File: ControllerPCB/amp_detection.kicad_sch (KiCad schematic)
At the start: 20 parts

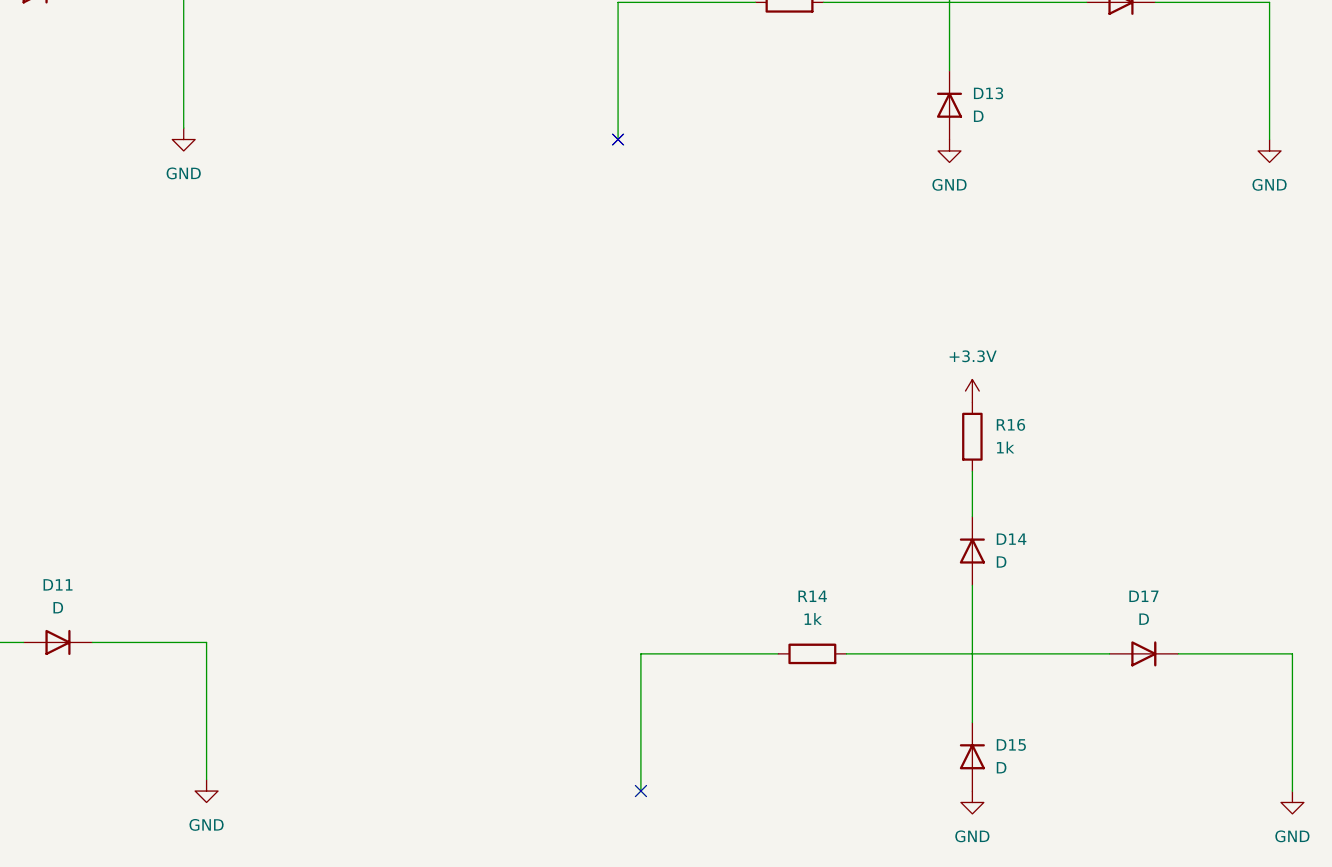
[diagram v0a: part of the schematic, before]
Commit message: Organized the schematic a bit
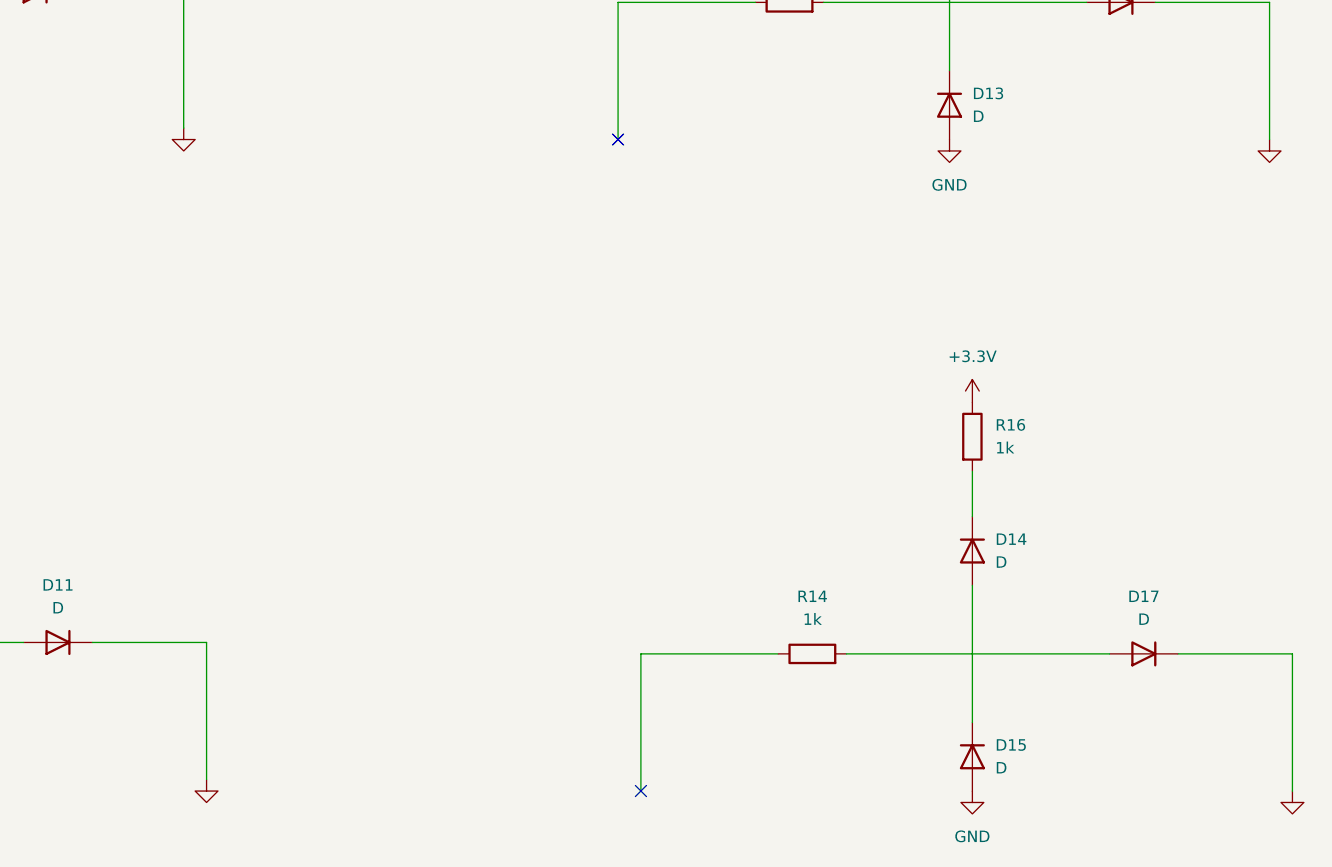
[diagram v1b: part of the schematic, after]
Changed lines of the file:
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@@
 					(size 1.27 1.27)
 				)
+				(hide yes)
 			)
 		)
@@
 					(size 1.27 1.27)
 				)
+				(hide yes)
 			)
 		)
@@
 					(size 1.27 1.27)
 				)
+				(hide yes)
 			)
 		)
@@
 					(size 1.27 1.27)
 				)
-			)
-		)
+				(hide yes)
+			)
+		)

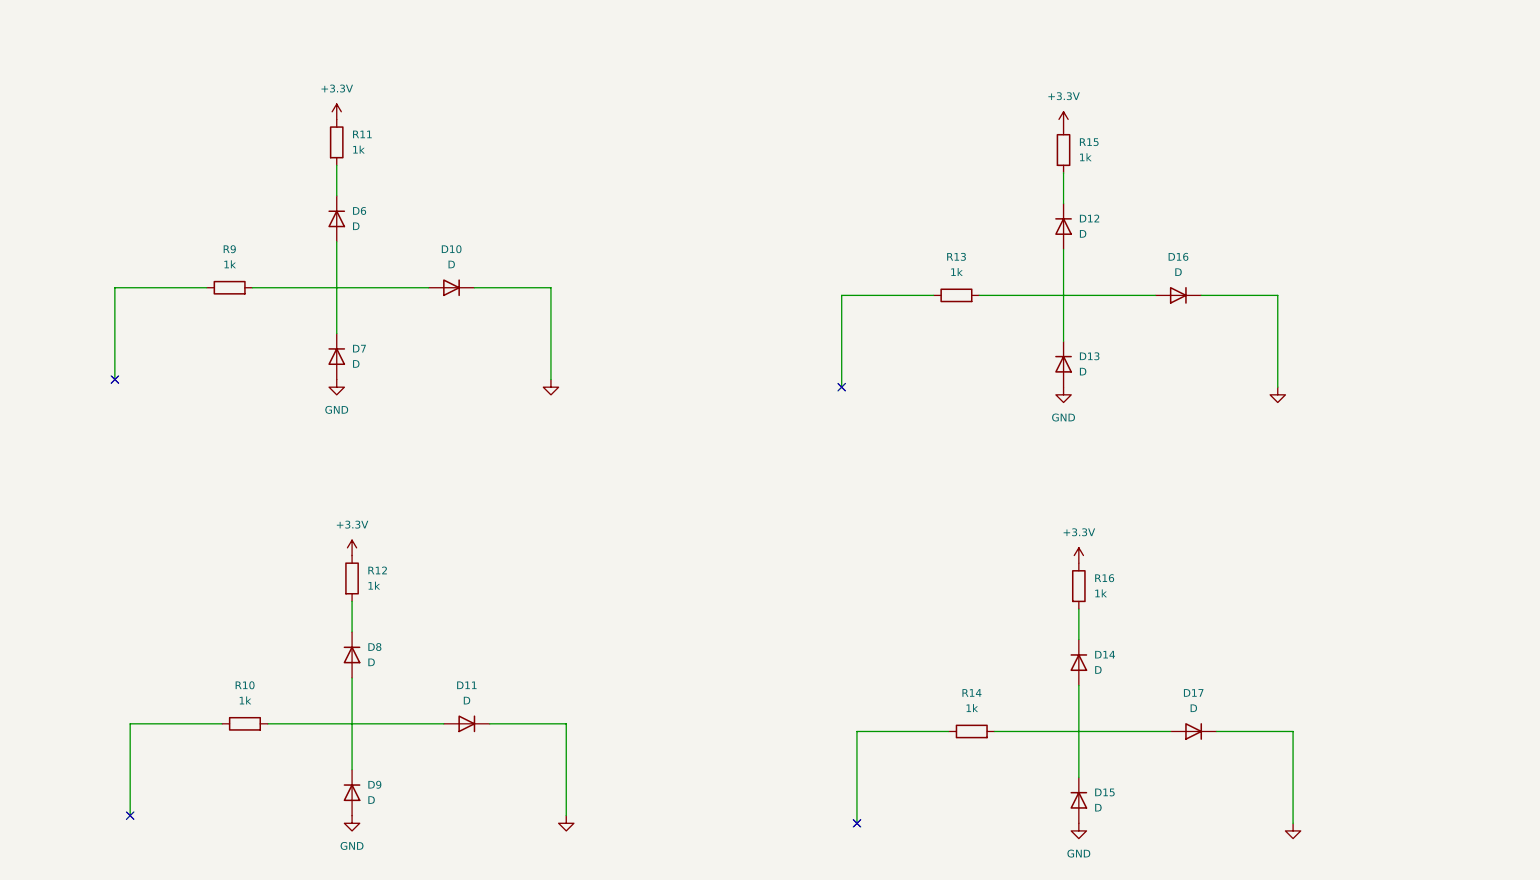
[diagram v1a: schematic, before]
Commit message: Began the PCB. Placed the decoupling caps, usb micro b conn and others. Adding footprints for components as well.
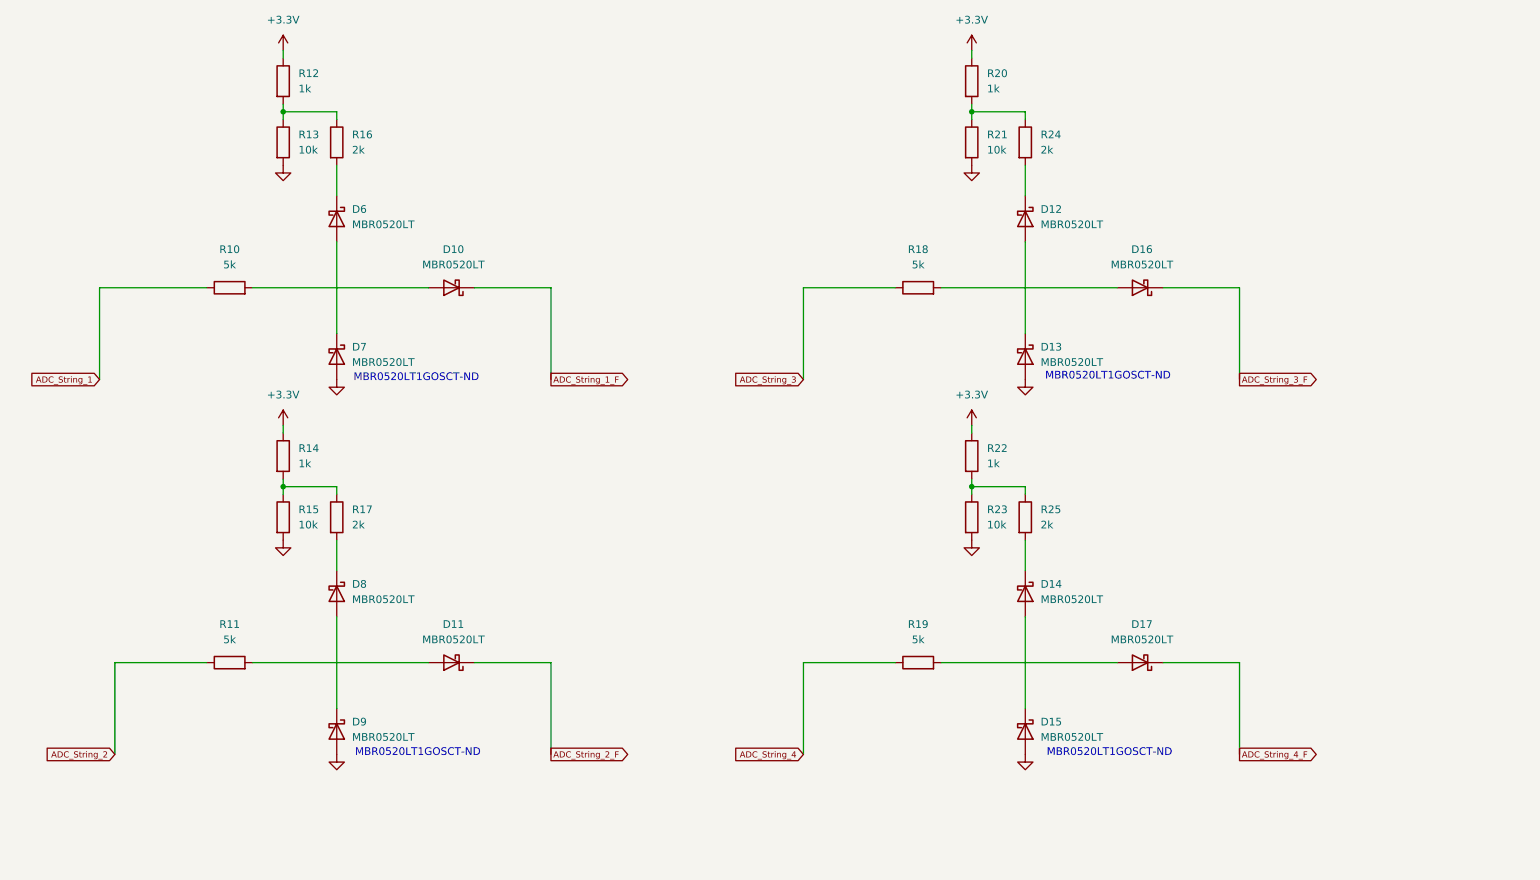
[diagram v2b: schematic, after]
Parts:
- removed D10, D11, D12, D13, D14, D15, D16, D17, D6, D7, D8, D9: D, symbol Device:D
- removed R10, R16: 1k, symbol Device:R
- added D10, D11, D12, D13, D14, D15, D16, D17, D6, D7, D8, D9: MBR0520LT, Diode_SMD:D_SOD-123, symbol Diode:MBR0520LT
- added R11, R18, R19: 5k, Resistor_SMD:R_0402_1005Metric, symbol Device:R
- added R17, R24, R25: 2k, Resistor_SMD:R_0402_1005Metric, symbol Device:R
- added R20, R22: 1k, Resistor_SMD:R_0402_1005Metric, symbol Device:R
- added R21, R23: 10k, Resistor_SMD:R_0402_1005Metric, symbol Device:R
- R10: renamed from R9; value 1k -> 5k; footprint (none) -> Resistor_SMD:R_0402_1005Metric
- R12, R14: footprint (none) -> Resistor_SMD:R_0402_1005Metric
- R13, R15: value 1k -> 10k; footprint (none) -> Resistor_SMD:R_0402_1005Metric
- R16: renamed from R11; value 1k -> 2k; footprint (none) -> Resistor_SMD:R_0402_1005Metric
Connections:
- net +3.3V: now also R14.1, R20.1, R22.1; no longer R15.1, R16.1
- net GND: now also R13.2, R15.2, D13.2 (A), D15.2 (A), D7.2 (A), D9.2 (A), R21.2, R23.2
- net at R16.2: now also D6.1 (K)
- net at R13.1: now also R12.2, R16.1
- net ADC_String_1: now reaches R10.1
- net at R10.2: now also D10.2 (A)
- net at R14.2: now also R15.1, R17.1
- new net: R22.2, R23.1, R25.1
- new net: D8.2 (A), D9.1 (K)
- new net: D17.2 (A), R19.2
- new net: D11.2 (A), R11.2
- new net: D14.2 (A), D15.1 (K)
- new net: D12.1 (K), R24.2
- new net: D12.2 (A), D13.1 (K)
- new net: D8.1 (K), R17.2
- new net: D14.1 (K), R25.2
- new net: D6.2 (A), D7.1 (K)
- new net: R20.2, R21.1, R24.1
- new net: D16.2 (A), R18.2
- new net ADC_String_1_F: D10.1 (K)
- new net ADC_String_2: R11.1
- new net ADC_String_2_F: D11.1 (K)
- new net ADC_String_3: R18.1
- new net ADC_String_3_F: D16.1 (K)
- new net ADC_String_4: R19.1
- new net ADC_String_4_F: D17.1 (K)
- no-connect marks 4 -> 0
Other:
- note added: "MBR0520LT1GOSCT-ND"

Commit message: Added separate sheet for IO. Added TVS diodes for every external input to the controller except for the ADC and MIDI control inputs. Still need to add decoupling caps for the 9V humbucker source. Parts were chosen with JLPCB library stock in mind. Replaced the 8MHz crystal with a 16MHz crystal.
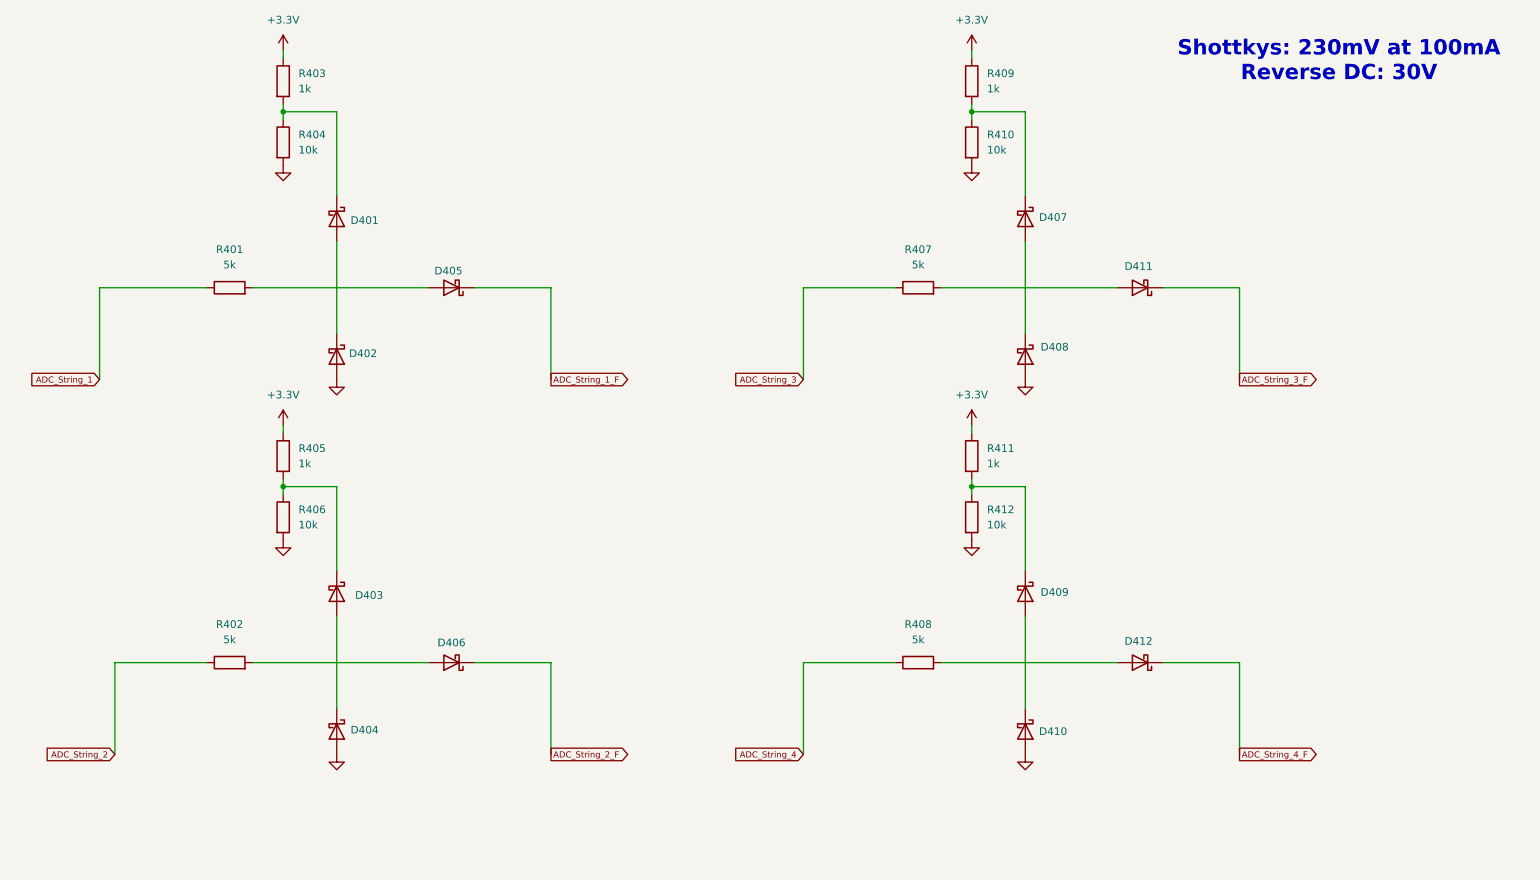
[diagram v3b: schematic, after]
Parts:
- removed R16, R17, R24, R25: 2k, Resistor_SMD:R_0402_1005Metric, symbol Device:R
- renumbered D6 to D401, D7 to D402, D8 to D403, D9 to D404, D10 to D405, D11 to D406, D12 to D407, D13 to D408, D14 to D409, D15 to D410, D16 to D411, D17 to D412, R10 to R401, R11 to R402, R12 to R403, R13 to R404, R14 to R405, R15 to R406, R18 to R407, R19 to R408, R20 to R409, R21 to R410, R22 to R411, R23 to R412
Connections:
- net at R411.2, R412.1: now also D409.1 (K)
- net at R403.2, R404.1: now also D401.1 (K)
- net at D407.1 (K): now also R409.2, R410.1
- net at R405.2, R406.1: now also D403.1 (K)
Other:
- note added: "Shottkys: 230mV at 100mA Reverse DC: 30V"
- note removed: "MBR0520LT1GOSCT-ND"

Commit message: rev 0.3
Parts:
- removed D401, D402, D403, D404, D405, D406, D407, D408, D409, D410, D411, D412: MBR0520LT, Diode_SMD:D_SOD-123, symbol Diode:MBR0520LT
- removed R402: 5k, Resistor_SMD:R_0402_1005Metric, symbol Device:R
- removed R405: 1k, Resistor_SMD:R_0402_1005Metric, symbol Device:R
- removed R406: 10k, Resistor_SMD:R_0402_1005Metric, symbol Device:R
- added C401, C402, C403, C404: 10n, Capacitor_SMD:C_0402_1005Metric, symbol Device:C
- added D401, D402, D403, D404, D405, D406, D407, D408, D409, D410, D411, D412: D_Small, Diode_SMD:D_SOD-323, symbol Device:D_Small
- added R401: 1k, Resistor_SMD:R_0402_1005Metric, symbol Device:R
- added R403: 220, Resistor_SMD:R_0402_1005Metric, symbol Device:R
- added R404: 2k, Resistor_SMD:R_0402_1005Metric, symbol Device:R
- R402: renamed from R401; value 5k -> 1k
- R405: renamed from R403; value 1k -> 220
- R406: renamed from R404; value 10k -> 2k
- R407: value 5k -> 1k
- R408: value 5k -> 220
- R409: value 1k -> 2k
- R410: value 10k -> 1k
- R411: value 1k -> 220
- R412: value 10k -> 2k
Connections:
- net +3.3V: now also R408.1, R403.1; no longer R409.1
- net ADC_String_1: now also C401.1
- net ADC_String_1_F: now also D406.1 (K)
- net ADC_String_2: now also C404.1, R401.1
- net ADC_String_2_F: now also D405.1 (K)
- net ADC_String_3: now also R410.1, C402.1; no longer R407.1
- net ADC_String_3_F: now also D412.1 (K)
- net ADC_String_4: now also R407.1, C403.1; no longer R408.1
- net ADC_String_4_F: now also D411.1 (K)
- net GND: now also R409.2, C401.2, C402.2, C403.2, C404.2, D402.1 (K), D404.1 (K), D408.1 (K), D410.1 (K), R404.2; no longer R410.2
- net 3V_OUT_3: now reaches R411.2, R412.1
- net 3V_OUT_3: now also D409.1 (K)
- net ADC_Diode_Net_1: now reaches R402.2
- net ADC_Diode_Net_1: now also D403.2 (A), D404.2 (A), D406.2 (A)
- net 3V_OUT_4: now reaches R408.2
- net 3V_OUT_4: now also R409.1, D407.1 (K)
- net 3V_OUT_1: now reaches R405.2, R406.1
- net 3V_OUT_1: now also D403.1 (K)
- net ADC_Diode_Net_4: now reaches R407.2
- net ADC_Diode_Net_4: now also D407.2 (A), D408.2 (A), D411.2 (A)
- new net 3V_OUT_2: D401.1 (K), R403.2, R404.1
- new net ADC_Diode_Net_2: D401.2 (A), D402.2 (A), D405.2 (A), R401.2
- new net ADC_Diode_Net_3: D409.2 (A), D410.2 (A), D412.2 (A), R410.2
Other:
- moved on the sheet: R402, R405, R406

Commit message: rev 0.4
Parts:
- removed C401, C402, C403, C404: 10n, Capacitor_SMD:C_0402_1005Metric, symbol Device:C
